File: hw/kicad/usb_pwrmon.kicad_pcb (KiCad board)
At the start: 2 copper layers, 45.2 x 21.8 mm, 33 parts, among them J1 ARM_10PIN, J2 USB_MALE_A, J3 USB_MICRO_B, J4 USB_FEMALE_A, SW1 SW_PUSH, U1 AD8293G80, U2 MKL24Z64VFM4

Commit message: - fix labels for usb dp/dm
Former-commit-id: 9a6132e0c8394671b9c07c581e160ab25a986f3f
Former-commit-id: d3e44395799e84ef5012f8b20a545457baf59de4
Former-commit-id: 0f8721ac38f384b7a2c523019ac0d14e291278d0
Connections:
- J3 pad 2: MON_USB_DM -> MON_USB_DP
- J4 pad 2: (no net) -> TRGT_USB_DP
- JP1 pad 1: MON_USB_DM -> MON_USB_DP
- JP3 pad 2: TRGT_USB_DM -> TRGT_USB_DP
- R4 pad 1: MON_USB_DM -> MON_USB_DP

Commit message: - more pcb
Former-commit-id: 2b197580a595ae499d754b0e2c51aaec8d6a7575
Former-commit-id: e6289b64b8c24ce4c0de00b1d0a4c61c2039cc18
Former-commit-id: c5622627f85b051a40ab499686b123414a3ac373
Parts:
- moved JP1 18.2 mm to (82.3, 34.8)
- moved JP2 17.1 mm to (83.8, 34.8)
- moved J2 1.09 mm to (74.9, 32.0)
- moved R6 0.51 mm to (93.5, 40.4), turned to 0 degrees
- moved J3 0.51 mm to (83.3, 41.7)
- moved SW1 0.25 mm to (102.9, 36.3)
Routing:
- net N-0000038: track 0.00 -> 19.3 mm
- net USB_DM: track 0.00 -> 6.35 mm, vias 0 -> 1
- net USB_DP: track 0.00 -> 3.85 mm, vias 0 -> 1
- net MON_USB_DM: track 0.00 -> 3.64 mm, vias 0 -> 1
- net MON_USB_DP: track 0.00 -> 3.60 mm, vias 0 -> 1
- net USB_VBUS: track 20.8 -> 20.2 mm
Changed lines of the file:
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@@
   (general
     (links 109)
-    (no_connects 107)
-    (area 62.733267 20.2836 130.25555 59.0154)
+    (no_connects 102)
+    (area 72.060999 21.006999 117.423001 43.001001)
     (thickness 1.6)
     (drawings 4)
-    (tracks 9)
+    (tracks 33)
     (zones 0)
     (modules 33)
@@
     (mod_text_size 1.5 1.5)
     (mod_text_width 0.15)
-    (pad_size 3.4 3.4)
-    (pad_drill 2)
+    (pad_size 1.75 1.1)
+    (pad_drill 0)
     (pad_to_mask_clearance 0.2)
     (aux_axis_origin 0 0)
@@
     )
   )
-  (module lvk12 (layer F.Cu)
-    (at 93.98 40.386 180)
-    (fp_text reference R6 (at -3.302 1.778 180) (layer F.SilkS)
-      (effects (font (size 0.75 0.75) (thickness 0.12)))
-    )
-    (fp_text value LVK12-SHUNT (at 0 -4.1 180) (layer F.SilkS) hide
-      (effects (font (size 1.5 1.5) (thickness 0.15)))
-    )
-    (pad 1 smd rect (at -1.375 -0.7 180) (size 1.75 1.1)
-      (layers F.Cu F.Paste F.Mask)
-      (net 34 USB_VBUS)
-    )
-    (pad 4 smd rect (at -1.375 0.7 180) (size 1.75 1.1)
-      (layers F.Cu F.Paste F.Mask)
-      (net 17 N-0000038)
-    )
-    (pad 2 smd rect (at 1.375 -0.7 180) (size 1.75 1.1)
-      (layers F.Cu F.Paste F.Mask)
-      (net 34 USB_VBUS)
-    )
-    (pad 3 smd rect (at 1.375 0.7 180) (size 1.75 1.1)
-      (layers F.Cu F.Paste F.Mask)
-      (net 17 N-0000038)
-    )
-  )
   (module jmp_small (layer B.Cu)
-    (at 66.294 43.434)
+    (at 82.296 34.798)
     (fp_text reference JP1 (at 0 2.032) (layer B.SilkS)
       (effects (font (size 0.75 0.75) (thickness 0.12)) (justify mirror))
@@
   )
   (module jmp_small (layer B.Cu)
-    (at 70.612 45.72)
+    (at 83.82 34.798)
     (fp_text reference JP2 (at 0 2.032) (layer B.SilkS)
       (effects (font (size 0.75 0.75) (thickness 0.12)) (justify mirror))
@@
   )
   (module usb_a_male_M701-280442 (layer F.Cu)
-    (at 74.295 31.115)
+    (at 74.93 32.004)
     (fp_text reference J2 (at 0.381 8.001) (layer F.SilkS)
       (effects (font (size 0.75 0.75) (thickness 0.12)))
@@
   )
   (module spst_pushbutton_smd (layer F.Cu)
-    (at 102.87 36.576 90)
+    (at 102.87 36.322 90)
     (fp_text reference SW1 (at 0.032 -1.686 90) (layer F.SilkS)
       (effects (font (size 0.75 0.75) (thickness 0.12)))
@@
   )
   (module usb_micro_b_smt (layer F.Cu)
-    (at 83.312 41.148)
+    (at 83.312 41.656)
     (fp_text reference J3 (at 5.334 -2.032) (layer F.SilkS)
       (effects (font (size 0.75 0.75) (thickness 0.12)))
@@
       (layers F.Cu F.Paste F.Mask)
       (net 34 USB_VBUS)
+    )
+  )
+  (module lvk12 (layer F.Cu)
+    (at 93.472 40.386)
+    (fp_text reference R6 (at 3.302 1.524) (layer F.SilkS)
+      (effects (font (size 0.75 0.75) (thickness 0.12)))
+    )
+    (fp_text value LVK12-SHUNT (at 0 -4.1) (layer F.SilkS) hide
+      (effects (font (size 1.5 1.5) (thickness 0.15)))
+    )
+    (pad 1 smd rect (at -1.375 -0.7) (size 1.75 1.1)
+      (layers F.Cu F.Paste F.Mask)
+      (net 34 USB_VBUS)
+    )
+    (pad 2 smd rect (at -1.375 0.7) (size 1.75 1.1)
+      (layers F.Cu F.Paste F.Mask)
+      (net 34 USB_VBUS)
+    )
+    (pad 4 smd rect (at 1.375 -0.7) (size 1.75 1.1)
+      (layers F.Cu F.Paste F.Mask)
+      (net 17 N-0000038)
+    )
+    (pad 3 smd rect (at 1.375 0.7) (size 1.75 1.1)
+      (layers F.Cu F.Paste F.Mask)
+      (net 17 N-0000038)
     )
   )
@@
   (gr_line (start 117.348 21.082) (end 117.348 42.926) (angle 90) (layer Edge.Cuts) (width 0.15))
   (gr_line (start 72.136 21.082) (end 117.348 21.082) (angle 90) (layer Edge.Cuts) (width 0.15))
+  (segment (start 83.312 38.656) (end 83.312 37.465) (width 0.254) (layer F.Cu) (net 8) (status 400000))
+  (segment (start 83.82 36.449) (end 83.82 35.433) (width 0.254) (layer B.Cu) (net 8) (status 800000))
+  (segment (start 84.074 36.703) (end 83.82 36.449) (width 0.254) (layer B.Cu) (net 8))
+  (via (at 84.074 36.703) (size 0.889) (layers F.Cu B.Cu) (net 8))
+  (segment (start 83.312 37.465) (end 84.074 36.703) (width 0.254) (layer F.Cu) (net 8))
+  (segment (start 82.662 38.656) (end 82.662 36.972) (width 0.254) (layer F.Cu) (net 9) (status 400000))
+  (segment (start 82.296 36.068) (end 82.296 35.433) (width 0.254) (layer B.Cu) (net 9) (status 800000))
+  (segment (start 82.931 36.703) (end 82.296 36.068) (width 0.254) (layer B.Cu) (net 9))
+  (via (at 82.931 36.703) (size 0.889) (layers F.Cu B.Cu) (net 9))
+  (segment (start 82.662 36.972) (end 82.931 36.703) (width 0.254) (layer F.Cu) (net 9))
+  (segment (start 94.847 41.086) (end 106.262 41.086) (width 0.5) (layer F.Cu) (net 17))
+  (segment (start 106.262 41.086) (end 111.844 35.504) (width 0.5) (layer F.Cu) (net 17))
+  (segment (start 83.82 34.163) (end 83.82 33.909) (width 0.254) (layer B.Cu) (net 32) (status C00000))
+  (segment (start 80.026 31.004) (end 78.93 31.004) (width 0.254) (layer F.Cu) (net 32) (status 800000))
+  (segment (start 80.772 31.75) (end 80.026 31.004) (width 0.254) (layer F.Cu) (net 32))
+  (via (at 80.772 31.75) (size 0.889) (layers F.Cu B.Cu) (net 32))
+  (segment (start 81.788 32.766) (end 80.772 31.75) (width 0.254) (layer B.Cu) (net 32))
+  (segment (start 82.677 32.766) (end 81.788 32.766) (width 0.254) (layer B.Cu) (net 32))
+  (segment (start 83.82 33.909) (end 82.677 32.766) (width 0.254) (layer B.Cu) (net 32) (status 400000))
+  (segment (start 78.93 33.004) (end 80.502 33.004) (width 0.254) (layer F.Cu) (net 33) (status 400000))
+  (segment (start 81.661 34.163) (end 82.296 34.163) (width 0.254) (layer B.Cu) (net 33) (status 800000))
+  (segment (start 80.899 33.401) (end 81.661 34.163) (width 0.254) (layer B.Cu) (net 33))
+  (via (at 80.899 33.401) (size 0.889) (layers F.Cu B.Cu) (net 33))
+  (segment (start 80.502 33.004) (end 80.899 33.401) (width 0.254) (layer F.Cu) (net 33))
   (segment (start 92.605 41.086) (end 90.87 41.086) (width 0.5) (layer F.Cu) (net 34))
   (segment (start 90.87 41.086) (end 89.916 40.132) (width 0.5) (layer F.Cu) (net 34))
@@
   (segment (start 87.376 35.814) (end 89.916 38.354) (width 0.5) (layer F.Cu) (net 34))
   (segment (start 79.494 35.814) (end 81.026 35.814) (width 0.5) (layer F.Cu) (net 34))
-  (segment (start 78.295 34.615) (end 79.494 35.814) (width 0.5) (layer F.Cu) (net 34))
-  (segment (start 82.012 36.8) (end 82.012 38.148) (width 0.5) (layer F.Cu) (net 34))
+  (segment (start 78.93 35.504) (end 79.494 35.814) (width 0.5) (layer F.Cu) (net 34) (status 10))
+  (segment (start 82.012 36.8) (end 82.012 38.656) (width 0.5) (layer F.Cu) (net 34) (status 20))
   (segment (start 81.026 35.814) (end 82.012 36.8) (width 0.5) (layer F.Cu) (net 34))
 )

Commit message: - update pcb
Former-commit-id: 3c17badaaac82903c2e47a4c7cb7e0bd24c2ef20
Former-commit-id: dc6542c9a6295d24b96af0493568a949c1ec9025
Former-commit-id: 85be3c60de07d725b23941281e7f28cccb11c1fc
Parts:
- removed J4: USB_FEMALE_A, usb_a_female_87520-0010BLF
- removed JP1, JP2, JP3, JP4: JUMPER, jmp_small
- removed J_2: OLED_FPC_CONN, oled_fpc_30
- removed R8: 10K, SM0603
- removed R9: 330R, SM0603
- added J_1: OLED_FPC_CONN, oled_fpc_30, F.Cu at (128.3, 43.4)
- added P1: TST, TEST_0.100, F.Cu at (112.0, 40.9)
- added P2: TST, TEST_0.100, F.Cu at (106.7, 43.9)
- added P3: TST, TEST_0.100, F.Cu at (124.0, 37.3)
- added P4: TST, TEST_0.100, F.Cu at (128.0, 37.3)
- added U3: AAT3221, SOT23-5, F.Cu at (119.9, 36.3)
- C1: value 2.2uF/16V -> 39nF
- C10: value 0.1uF -> 1uF
- C11: value 0.1uF -> 10uF
- C2: value 1uF -> 0.1uF
- C3: value 1uF -> 1300pF
- C6: value 10uF -> 2.2uF/16V
- C7: value 2.2uF -> 1uF
- C8: value 39nF -> 1uF
- C9: value 1300pF -> 1uF
- J3: value USB_MICRO_B -> USB_FEMALE_A; footprint usb_micro_b_smt -> usb_female_a
- R1: value 390K -> 25K
- R2: value 25K -> 8K
- R3: value 8K -> 330R
- R4: value 33R -> LVK12-SHUNT; footprint SM0603 -> lvk12
- R5: value 33R -> 25K
- R6: value LVK12-SHUNT -> 25K; footprint lvk12 -> SM0603
- R7: value 10K -> 390K
- U2: value MKL24Z64VFM4 -> MKL02ZXVFG4; footprint MKL24Z64VFM4 -> MKL02_QFN16
- moved U2 32.9 mm to (117.4, 43.0), turned to 0 degrees
- moved J3 30.3 mm to (112.0, 32.0), turned to 90 degrees
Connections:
- C1 pad 2: N-0000047 -> ADC_OUT
- C10 pad 1: USB_VBUS -> GND
- C10 pad 2: GND -> +3.3
- C11 pad 1: NRESET -> GND
- C11 pad 2: GND -> N-0000040
- C2 pad 1: N-0000043 -> NRESET
- C2 pad 2: N-0000050 -> GND
- C3 pad 1: N-0000042 (its old number) -> N-0000013
- C3 pad 2: N-0000049 -> N-0000012
- C4 pad 1: GND -> USB_VBUS
- C4 pad 2: +3.3 -> GND
- C5 pad 1: GND -> +3.3
- C5 pad 2: +3.3 -> GND
- C7 pad 1: +3.3v -> N-0000035
- C7 pad 2: GND -> N-0000038
- C8 pad 1: GND -> N-0000034
- C8 pad 2: ADC_OUT -> N-0000036
- C9 pad 1: N-0000011 -> GND
- C9 pad 2: N-0000010 -> +3.3
- D1 pad 1: N-0000013 -> N-0000017
- D1 pad 2: N-0000014 -> N-000005
- J3 pad 1: USB_VBUS -> N-0000029
- J3 pad 2: MON_USB_DP -> USB_DP
- J3 pad 3: MON_USB_DM -> USB_DM
- J3 pad 4: (no net) -> GND
- R1 pad 1: GND -> N-0000010
- R1 pad 2: N-0000048 -> +3.3v
- R2 pad 1: N-0000012 -> N-0000010
- R2 pad 2: +3.3v -> GND
- R3 pad 1: N-0000012 -> N-000005
- R4 pad 1: MON_USB_DP -> USB_VBUS
- R4 pad 2: N-000006 -> USB_VBUS
- R5 pad 1: MON_USB_DM -> USB_VBUS
- R5 pad 2: N-000007 -> VBUS_SENSE
- R6 pad 1: USB_VBUS -> VBUS_SENSE
- R6 pad 2: USB_VBUS -> GND
- R7 pad 1: USB_VBUS -> GND
- R7 pad 2: N-0000030 -> N-0000037
- SW1 pad 2: N-0000021 -> N-0000011
- U1 pad 3: N-0000012 -> N-0000010
- U1 pad 5: N-0000010 -> N-0000012
- U1 pad 6: N-0000011 -> N-0000013
- U1 pad 8: N-0000038 -> N-0000029
- U2 pad 1: (no net) -> +3.3v
- U2 pad 10: SWCLK -> ADC_OUT
- U2 pad 11: N-0000013 -> SERIAL_TX
- U2 pad 12: (no net) -> SERIAL_RX
- U2 pad 13: SWDIO -> (no net)
- U2 pad 14: (no net) -> SWCLK
- U2 pad 15: +3.3v -> NRESET
- U2 pad 16: GND -> SWDIO
- U2 pad 3: N-000006 -> N-0000011
- U2 pad 4: N-000007 -> N-0000017
- U2 pad 5: +3.3v -> (no net)
- U2 pad 6: USB_VBUS -> (no net)
- U2 pad 7: +3.3v -> (no net)
- U2 pad 8: GND -> (no net)
- U2 pad 9: N-0000030 -> VBUS_SENSE
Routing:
- net N-0000038: track 19.3 -> 0.00 mm
- net N-0000029: track 0.00 -> 19.3 mm
- net USB_DM: track 6.35 -> 0.00 mm, vias 1 -> 0
- net USB_DP: track 3.85 -> 0.00 mm, vias 1 -> 0
- net MON_USB_DM: track 3.64 -> 0.00 mm, vias 1 -> 0
- net MON_USB_DP: track 3.60 -> 0.00 mm, vias 1 -> 0

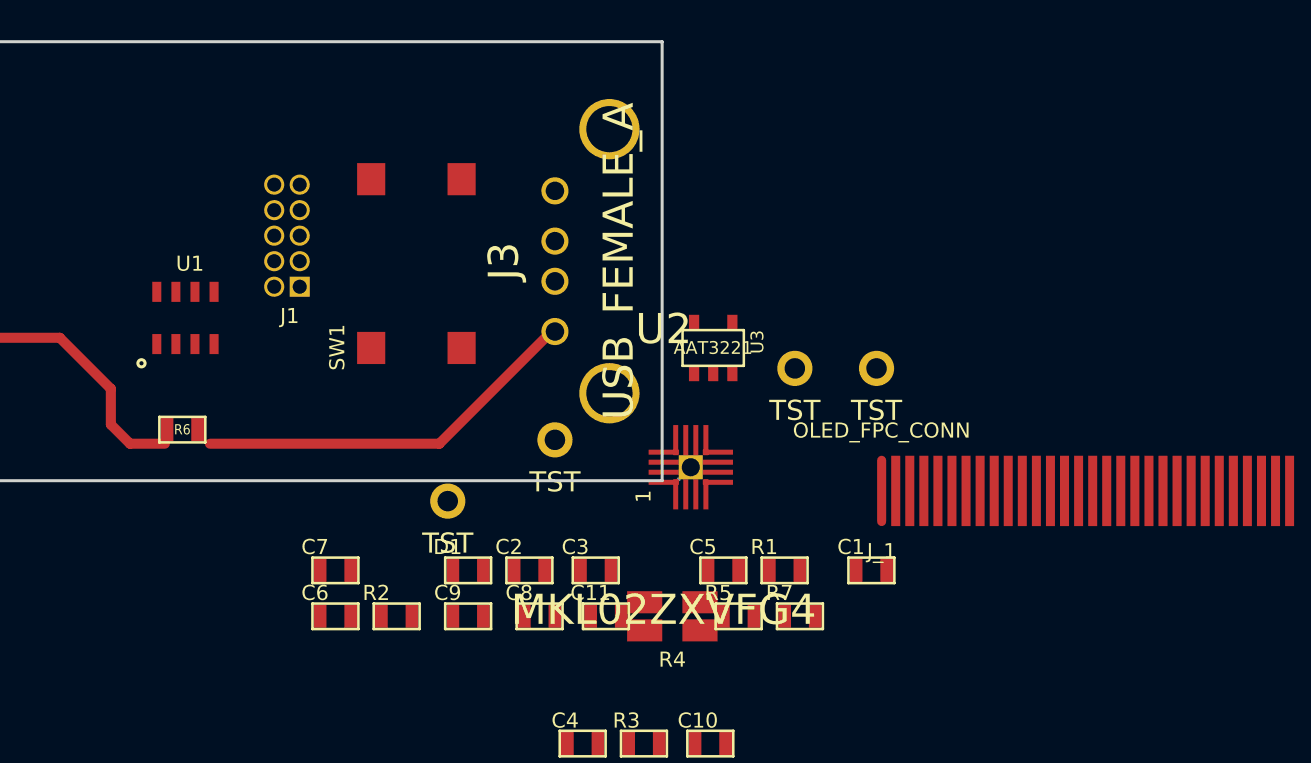
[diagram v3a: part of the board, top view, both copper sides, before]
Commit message: - fix some components, switch to smt 10 pin debug header
Former-commit-id: fe5513d4f7cfa6e60e96780276d93b6a6b08847d
Former-commit-id: e371d3e6ef20b5cd06e2b546f1efa9134f2f16a7
Former-commit-id: 2d63e4279259ba7f4e4f789c992275eb97b1c8aa
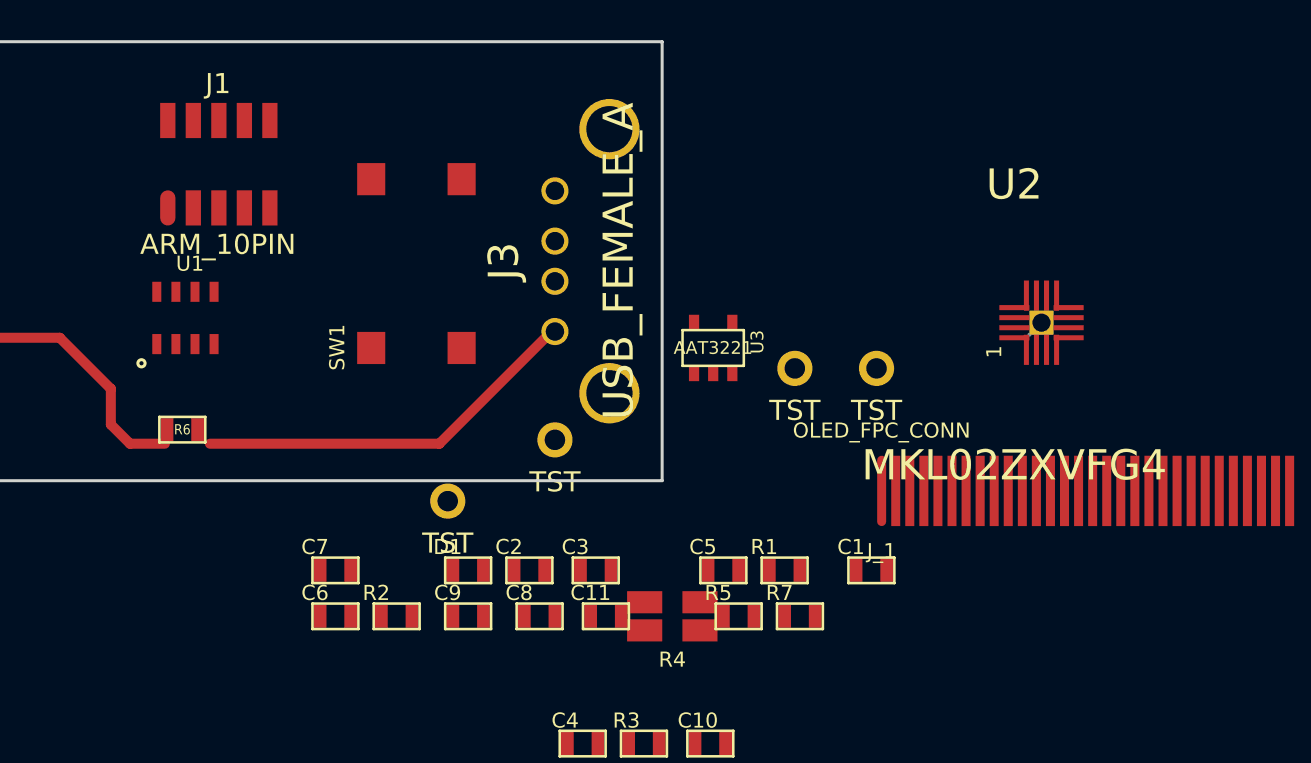
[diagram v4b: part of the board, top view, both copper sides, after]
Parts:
- J1: footprint ARM_10_PIN -> ARM_10_PIN_SMT
- moved U2 18.9 mm to (134.9, 35.8)
- moved J1 5.40 mm to (95.2, 27.2), turned to 0 degrees
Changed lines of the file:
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@@
-    )
-  )
-  (module ARM_10_PIN (layer F.Cu)
-    (at 99.314 30.734 180)
-    (fp_text reference J1 (at 0.5 -4 180) (layer F.SilkS)
-      (effects (font (size 0.75 0.75) (thickness 0.12)))
-    )
-    (fp_text value ARM_10PIN (at 1 4 180) (layer F.SilkS) hide
-      (effects (font (size 1 1) (thickness 0.15)))
-    )
-    (pad 1 thru_hole rect (at 0 -2.54 180) (size 1 1) (drill 0.70104)
-      (layers *.Cu *.Mask F.SilkS)
-      (net 2 +3.3v)
-    )
-    (pad 2 thru_hole circle (at 1.27 -2.54 180) (size 1 1) (drill 0.70104)
-      (layers *.Cu *.Mask F.SilkS)
-      (net 23 SWDIO)
-    )
-    (pad 3 thru_hole circle (at 0 -1.27 180) (size 1 1) (drill 0.70104)
-      (layers *.Cu *.Mask F.SilkS)
-      (net 4 GND)
-    )
-    (pad 4 thru_hole circle (at 1.27 -1.27 180) (size 1 1) (drill 0.70104)
-      (layers *.Cu *.Mask F.SilkS)
-      (net 22 SWCLK)
-    )
-    (pad 5 thru_hole circle (at 0 0 180) (size 1 1) (drill 0.70104)
-      (layers *.Cu *.Mask F.SilkS)
-      (net 4 GND)
-    )
-    (pad 6 thru_hole circle (at 1.27 0 180) (size 1 1) (drill 0.70104)
-      (layers *.Cu *.Mask F.SilkS)
-    )
-    (pad 7 thru_hole circle (at 0 1.27 180) (size 1 1) (drill 0.70104)
-      (layers *.Cu *.Mask F.SilkS)
-    )
-    (pad 8 thru_hole circle (at 1.27 1.27 180) (size 1 1) (drill 0.70104)
-      (layers *.Cu *.Mask F.SilkS)
-    )
-    (pad 9 thru_hole circle (at 0 2.54 180) (size 1 1) (drill 0.70104)
-      (layers *.Cu *.Mask F.SilkS)
-      (net 4 GND)
-    )
-    (pad 10 thru_hole circle (at 1.27 2.54 180) (size 1 1) (drill 0.70104)
-      (layers *.Cu *.Mask F.SilkS)
-      (net 19 NRESET)
     )
   )
@@
   )
   (module MKL02_QFN16 (layer F.Cu)
-    (at 117.423001 43.006001)
+    (at 134.874 35.814)
     (fp_text reference U2 (at 0 -7.62) (layer F.SilkS)
       (effects (font (size 1.5 1.5) (thickness 0.15)))
@@
     )
   )
+  (module ARM_10_PIN_SMT (layer F.Cu)
+    (at 95.25 27.178)
+    (fp_text reference J1 (at 0 -4) (layer F.SilkS)
+      (effects (font (size 1 1) (thickness 0.15)))
+    )
+    (fp_text value ARM_10PIN (at 0 4) (layer F.SilkS)
+      (effects (font (size 1 1) (thickness 0.15)))
+    )
+    (pad 1 smd oval (at -2.5 2.175) (size 0.76 1.75)
+      (layers F.Cu F.Paste F.Mask)
+      (net 2 +3.3v)
+    )
+    (pad 2 smd rect (at -2.5 -2.175) (size 0.76 1.75)
+      (layers F.Cu F.Paste F.Mask)
+      (net 23 SWDIO)
+    )
+    (pad 3 smd rect (at -1.23 2.175) (size 0.76 1.75)
+      (layers F.Cu F.Paste F.Mask)
+      (net 4 GND)
+    )
+    (pad 4 smd rect (at -1.23 -2.175) (size 0.76 1.75)
+      (layers F.Cu F.Paste F.Mask)
+      (net 22 SWCLK)
+    )
+    (pad 5 smd rect (at 0.04 2.175) (size 0.76 1.75)
+      (layers F.Cu F.Paste F.Mask)
+      (net 4 GND)
+    )
+    (pad 6 smd rect (at 0.04 -2.175) (size 0.76 1.75)
+      (layers F.Cu F.Paste F.Mask)
+    )
+    (pad 7 smd rect (at 1.31 2.175) (size 0.76 1.75)
+      (layers F.Cu F.Paste F.Mask)
+    )
+    (pad 8 smd rect (at 1.31 -2.175) (size 0.76 1.75)
+      (layers F.Cu F.Paste F.Mask)
+    )
+    (pad 9 smd rect (at 2.58 2.175) (size 0.76 1.75)
+      (layers F.Cu F.Paste F.Mask)
+      (net 4 GND)
+    )
+    (pad 10 smd rect (at 2.58 -2.175) (size 0.76 1.75)
+      (layers F.Cu F.Paste F.Mask)
+      (net 19 NRESET)
+    )
+  )
